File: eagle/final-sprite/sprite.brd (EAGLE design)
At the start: 35 x 44.6 mm, 60 parts, among them J1 M20-7910442R, U1 CC430F513X, U2 LSM9DS1, U4 DRV8837, U5 ADP5092, U6 DRV8837, U7 DRV8837, X1 SPRITEPIN_SPRITE_PIN, X2 SPRITEPIN_SPRITE_PIN

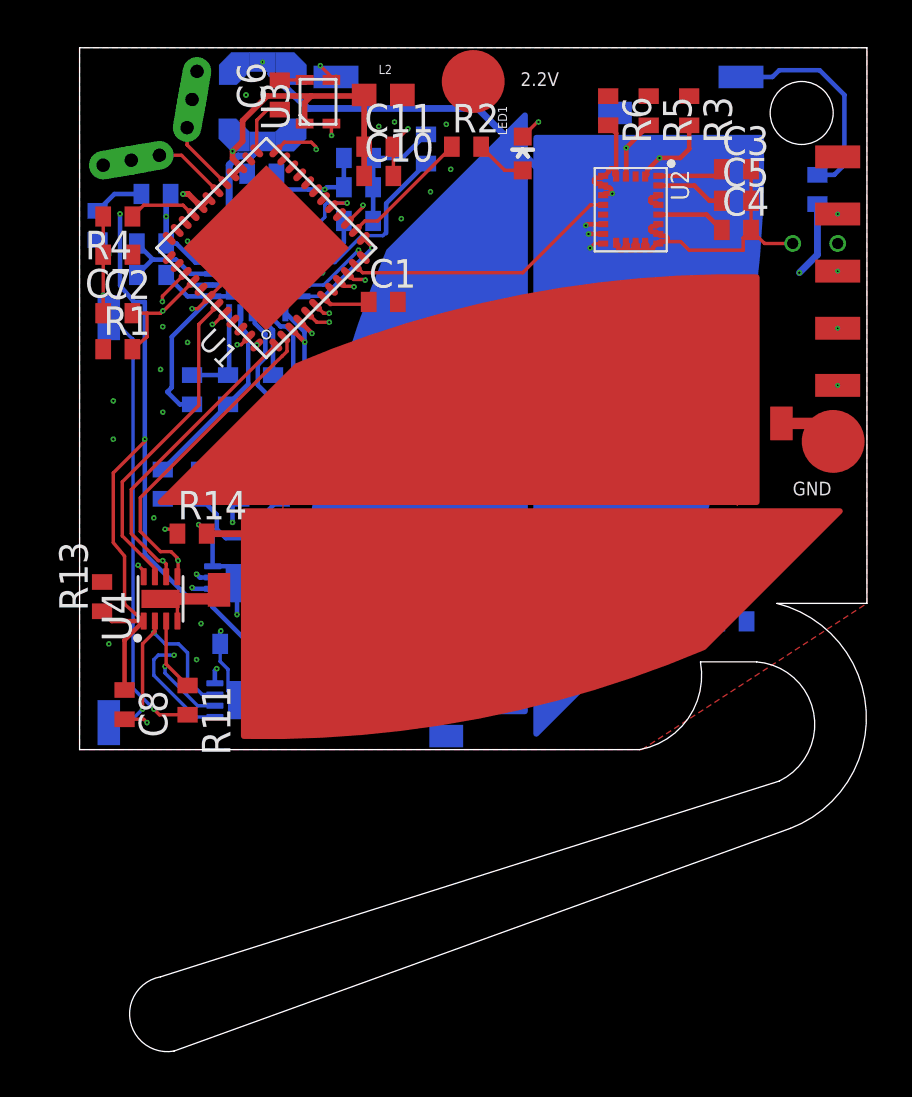
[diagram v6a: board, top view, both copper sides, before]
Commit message: moved all 3 drivers to the bottom side, removed the need for using interlayers and decreased the total number of vias
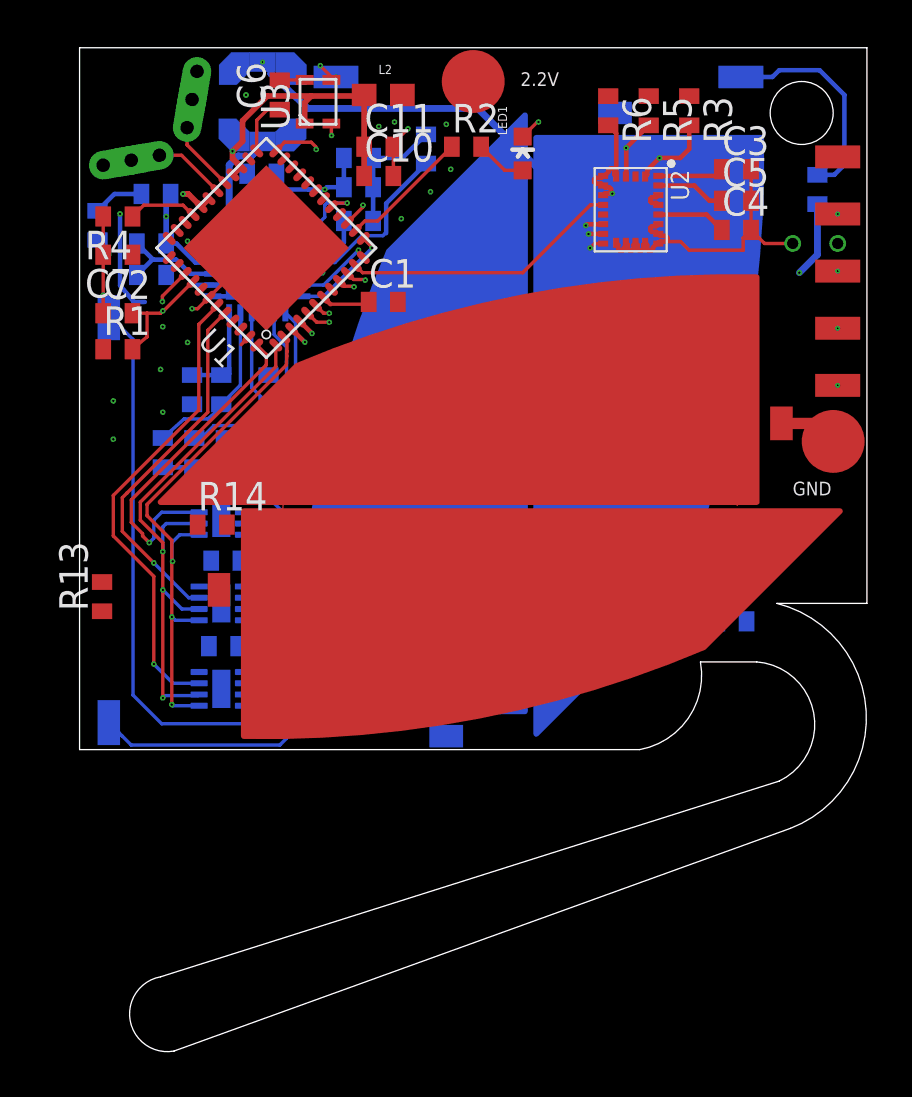
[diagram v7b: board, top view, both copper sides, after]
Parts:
- moved C8 5.11 mm to (6.40, 8.40), flipped to the bottom, turned to 0 degrees
- moved U4 4.83 mm to (6.30, 6.50), flipped to the bottom, turned to 0 degrees
- moved U6 4.36 mm to (6.30, 10.3)
- moved R11 3.72 mm to (8.50, 5.60), flipped to the bottom
- moved C12 3.72 mm to (6.50, 12.2)
- moved U7 2.96 mm to (6.30, 14.1), turned to 0 degrees
- moved R18 1.72 mm to (7.90, 17.0)
- moved R19 1.52 mm to (6.50, 17.0)
- moved R20 1.43 mm to (5.10, 17.0)
- moved R15 1.40 mm to (3.70, 17.0)
- moved R14 0.98 mm to (5.90, 13.8)
- moved R16 0.30 mm to (6.30, 19.8)
- moved R21 0.20 mm to (8.40, 19.8)
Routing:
- net GND: track 77.5 -> 46.9 mm, vias 11 -> 6
- net VCCIO: track 48.3 -> 27.6 mm, vias 3 -> 2
- net N$14: track 5.89 -> 13.1 mm, vias 1 -> 0
- net EN_1: track 14.4 -> 21.0 mm, vias 0 -> 1
- net PWM2: track 28.9 -> 24.2 mm
- net VCC: track 17.6 -> 13.3 mm, vias 21 -> 13
- net REF: track 16.8 -> 12.5 mm
- net PWM1: track 29.2 -> 25.0 mm
- net EN_2: track 20.4 -> 16.2 mm, vias 2 -> 1
- net N$4: track 19.9 -> 23.9 mm, vias 1 -> 0
- net VCCINT: track 41.0 -> 38.4 mm
- net N$8: track 3.26 -> 1.21 mm
- net TERM: track 9.99 -> 8.52 mm
- net SETSD: track 9.52 -> 8.12 mm
- net EN_3: track 14.1 -> 15.1 mm, vias 2 -> 1
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- removed copper zone on layer 2, net GND
- removed copper zone on layer 1, net VCC
- removed copper zone on layer 3, net VCC

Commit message: added new trisol footprint to layout
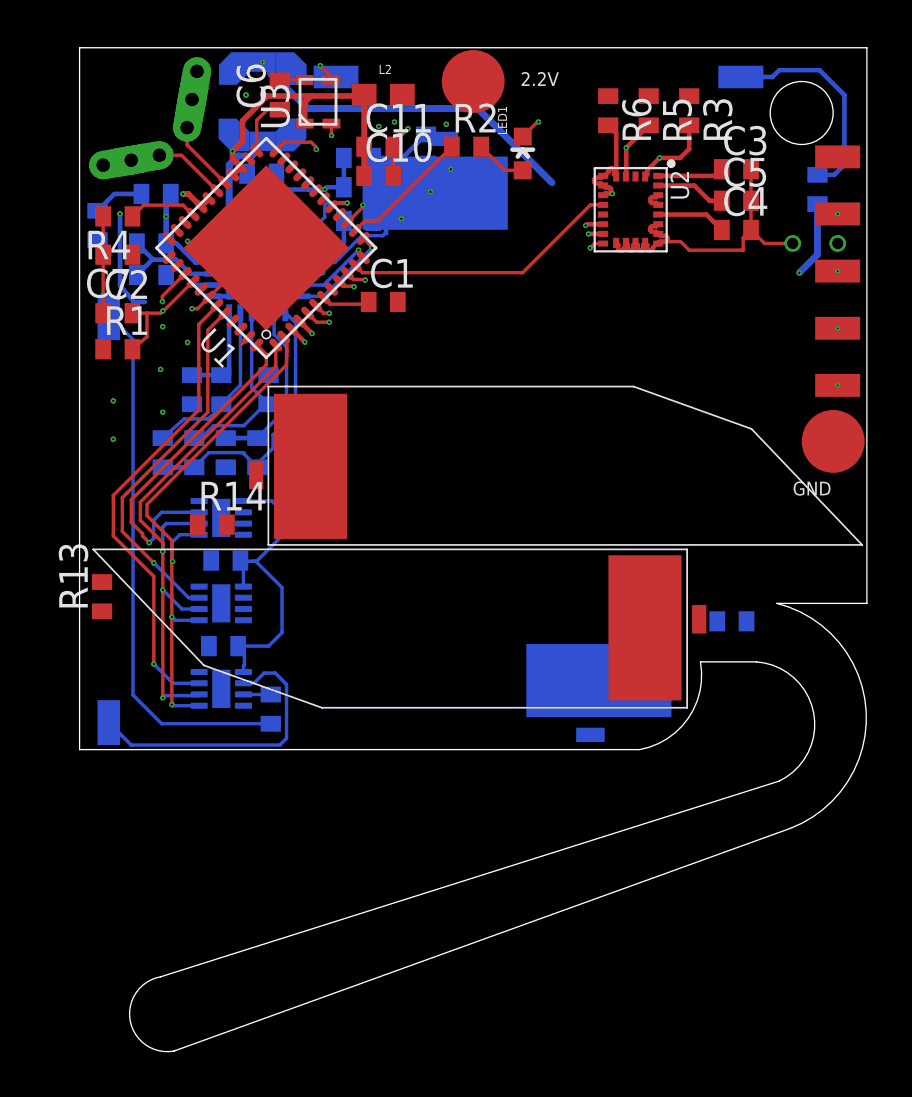
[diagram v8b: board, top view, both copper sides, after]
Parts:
- D1, D2, D3, D4: value TRISOLX-WING -> TRISOLX-WINGSTRAIGHT-RS; device STAC:TRISOLX_QZQUBE_TRISOLX-T01 -> STAC:TRISOLX-STRAIGHT-RS
- moved D4 14.2 mm to (22.2, 16.9)
- moved D3 13.4 mm to (16.7, 18.5)
- moved D2 9.82 mm to (20.3, 15.5)
- moved D1 8.91 mm to (15.1, 10.1)
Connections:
- net GND: now also D1.P$2, D2.P$2, D3.P$2, D4.P$2; no longer D1.P$3, D2.P$3, D3.P$3, D4.P$3
- net VCCINT: now also D1.P$1, D2.P$1, D3.P$1, D4.P$1; no longer D1.P$2, D2.P$2, D3.P$2, D4.P$2
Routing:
- net VCCINT: track 38.4 -> 29.7 mm
- net GND: track 46.9 -> 45.4 mm
- removed copper zone on layer 1, net VCCINT
- removed copper zone on layer 16, net VCCINT
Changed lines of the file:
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@@
 <element name="X2" library="STAC" package="SPRITEPIN_SPRITE_PIN" value="SPRITEPIN_SPRITE_PIN" x="33.5" y="17.5"/>
 <element name="B1" library="STAC" package="UMAC_UMAC" value="UMAC_UMAC" x="32.7" y="23.8" rot="MR90"/>
-<element name="D1" library="STAC" package="TRISOLX_QZQUBE_TRISOLX-T01" value="TRISOLX-WING" x="7.3" y="14.4" rot="R180"/>
-<element name="D2" library="STAC" package="TRISOLX_QZQUBE_TRISOLX-T01" value="TRISOLX-WING" x="30.1" y="14.8"/>
-<element name="D3" library="STAC" package="TRISOLX_QZQUBE_TRISOLX-T01" value="TRISOLX-WING" x="19.8" y="5.5" rot="MR270"/>
-<element name="D4" library="STAC" package="TRISOLX_QZQUBE_TRISOLX-T01" value="TRISOLX-WING" x="20.3" y="31" rot="MR90"/>
+<element name="D2" library="STAC" package="TRISOLX-STRAIGHT-RS" value="TRISOLX-WINGSTRAIGHT-RS" x="20.3" y="15.5"/>
+<element name="D3" library="STAC" package="TRISOLX-STRAIGHT-RS" value="TRISOLX-WINGSTRAIGHT-RS" x="16.7" y="18.5" rot="MR270"/>
+<element name="D4" library="STAC" package="TRISOLX-STRAIGHT-RS" value="TRISOLX-WINGSTRAIGHT-RS" x="22.2" y="16.9" rot="MR90"/>
 <element name="U3" library="STAC" package="SPRITETCXO_TXC_7Z" value="" x="10.6" y="32.6" rot="R90"/>
 <element name="U1" library="STAC" package="TI_MSP430_V16_RGZ48" value="CC430F513X" x="8.3" y="26.1" rot="R135"/>
@@
 <element name="L3" library="STAC" package="PCBSAT-TORQUECOIL" value="PCBSAT-TORQUECOIL" x="1.3" y="14" rot="MR270"/>
 <element name="L4" library="STAC" package="PCBSAT-TORQUECOIL" value="PCBSAT-TORQUECOIL" x="20.4" y="33.7" rot="MR0"/>
+<element name="D1" library="STAC" package="TRISOLX-STRAIGHT-RS" value="TRISOLX-WINGSTRAIGHT-RS" x="15.1" y="10.1" rot="R180"/>
 </elements>
 <signals>
@@
 <contactref element="X2" pad="PIN"/>
 <contactref element="B1" pad="V-"/>
-<contactref element="D1" pad="P$3"/>
-<contactref element="D2" pad="P$3"/>
-<contactref element="D3" pad="P$3"/>
-<contactref element="D4" pad="P$3"/>
+<contactref element="D2" pad="P$2"/>
+<contactref element="D3" pad="P$2"/>
+<contactref element="D4" pad="P$2"/>
 <contactref element="U3" pad="GND2"/>
 <contactref element="U3" pad="GND1"/>
@@
 <wire x1="26.717" y1="26.383" x2="27.1" y2="26" width="0.1524" layer="1"/>
 <wire x1="33.5" y1="17.5" x2="32.7" y2="18.3" width="0.508" layer="1"/>
-<wire x1="32.7" y1="18.3" x2="31.2" y2="18.3" width="0.508" layer="1"/>
 <wire x1="29.85" y1="26.9" x2="30.45" y2="26.3" width="0.1524" layer="1"/>
 <wire x1="30.45" y1="26.3" x2="31.7" y2="26.3" width="0.1524" layer="1"/>
@@
 <wire x1="11.195" y1="33.705" x2="10.7" y2="34.2" width="0.1524" layer="1"/>
 <via x="10.7" y="34.2" extent="1-2" drill="0.1016"/>
-<wire x1="20.4" y1="31.7" x2="23.8" y2="32.1" width="0" layer="19" extent="2-16"/>
+<contactref element="D1" pad="P$2"/>
+<wire x1="33.5" y1="17.5" x2="33.7" y2="17.45" width="0" layer="19" extent="1-1"/>
+<wire x1="31.7" y1="26.3" x2="32.7" y2="18.3" width="0" layer="19" extent="1-1"/>
+<wire x1="23.089" y1="6.867" x2="24.01739375" y2="25.973" width="0" layer="19" extent="1-16"/>
+<wire x1="15.811" y1="28.533" x2="23.089" y2="6.867" width="0" layer="19" extent="16-16"/>
+<wire x1="19.7" y1="31.05" x2="23.855" y2="26.325" width="0" layer="19" extent="1-1"/>
 <wire x1="15.4" y1="31.15" x2="19.7" y2="31.05" width="0" layer="19" extent="1-16"/>
 <wire x1="13.95" y1="30.6" x2="14.35" y2="30.1" width="0" layer="19" extent="1-16"/>
@@
 <wire x1="7.285" y1="13.35" x2="6.3" y2="14.1" width="0" layer="19" extent="16-16"/>
 <wire x1="5.85" y1="12.2" x2="7.285" y2="13.35" width="0" layer="19" extent="16-16"/>
-<wire x1="6.2" y1="10.9" x2="5.85" y2="12.2" width="0" layer="19" extent="1-16"/>
-<wire x1="6.3" y1="10.3" x2="6.2" y2="10.9" width="0" layer="19" extent="1-16"/>
+<wire x1="6.3" y1="10.3" x2="5.85" y2="12.2" width="0" layer="19" extent="16-16"/>
 <wire x1="7.285" y1="9.55" x2="6.3" y2="10.3" width="0" layer="19" extent="16-16"/>
 <wire x1="5.75" y1="8.4" x2="7.285" y2="9.55" width="0" layer="19" extent="16-16"/>
@@
 <wire x1="7.285" y1="5.75" x2="6.3" y2="6.5" width="0" layer="19" extent="16-16"/>
 <wire x1="14.15" y1="23.7" x2="13.05" y2="27.3" width="0" layer="19" extent="1-16"/>
-<wire x1="25.44739375" y1="27.067" x2="23.8" y2="32.1" width="0" layer="19" extent="1-16"/>
-<wire x1="31.2" y1="18.3" x2="29.5" y2="26" width="0" layer="19" extent="1-1"/>
-<wire x1="33.7" y1="17.45" x2="33.5" y2="17.5" width="0" layer="19" extent="1-1"/>
-<wire x1="16.3" y1="4.4" x2="7.285" y2="5.75" width="0" layer="19" extent="16-16"/>
+<wire x1="10.267" y1="16.389" x2="6.5" y2="16.35" width="0" layer="19" extent="1-16"/>
+<wire x1="25.133" y1="9.211" x2="7.285" y2="5.75" width="0" layer="19" extent="1-16"/>
 </signal>
 <signal name="N$3">
@@
 <contactref element="C17" pad="1"/>
 <contactref element="R14" pad="2"/>
-<contactref element="D1" pad="P$2"/>
-<contactref element="D2" pad="P$2"/>
-<contactref element="D3" pad="P$2"/>
-<contactref element="D4" pad="P$2"/>
+<contactref element="D2" pad="P$1"/>
+<contactref element="D3" pad="P$1"/>
+<contactref element="D4" pad="P$1"/>
 <wire x1="3.85" y1="26.3" x2="3.85" y2="27.5" width="0.254" layer="16"/>
 <wire x1="4.05" y1="28.5" x2="3.85" y2="28.3" width="0.254" layer="16"/>
@@
 <wire x1="8.509903125" y1="33.843653125" x2="8.51289375" y2="33.8406625" width="0.3048" layer="16"/>
 <wire x1="8.5735375" y1="33.78001875" x2="10.15355625" y2="32.3" width="0.3048" layer="16"/>
-<wire x1="21" y1="29" x2="25.3" y2="29" width="0.3048" layer="16"/>
 <wire x1="10.15355625" y1="32.3" x2="17.7" y2="32.3" width="0.3048" layer="16"/>
 <wire x1="17.7" y1="32.3" x2="21" y2="29" width="0.3048" layer="16"/>
-<polygon width="0.3048" layer="16">
-<vertex x="19.8" y="31"/>
-<vertex x="25.9" y="29.5"/>
-<vertex x="25.5" y="10.6"/>
-<vertex x="13" y="6.3"/>
-<vertex x="19.9" y="30.9"/>
-</polygon>
-<polygon width="0.3048" layer="1" thermals="no">
-<vertex x="8.3" y="5.5"/>
-<vertex x="9.5" y="20.2"/>
-<vertex x="29.3" y="21.3"/>
-<vertex x="29.2" y="11"/>
-</polygon>
 <wire x1="5.92" y1="25.45" x2="5.15" y2="25.45" width="0.2032" layer="16"/>
 <wire x1="4.3" y1="26.3" x2="3.85" y2="26.3" width="0.2032" layer="16"/>
 <wire x1="5.15" y1="25.45" x2="4.3" y2="26.3" width="0.2032" layer="16"/>
-<wire x1="8.2" y1="13.4" x2="8.2" y2="10.5" width="0.3048" layer="1"/>
-<wire x1="8.2" y1="10.5" x2="9.3" y2="9.4" width="0.3048" layer="1"/>
-<wire x1="25.3" y1="29" x2="28.1" y2="19.8" width="0" layer="19" extent="1-16"/>
-<wire x1="6.55" y1="13.8" x2="5.92" y2="25.45" width="0" layer="19" extent="1-16"/>
-<wire x1="8.2" y1="13.4" x2="6.55" y2="13.8" width="0" layer="19" extent="1-1"/>
-<wire x1="14.8" y1="7.5" x2="9.3" y2="9.4" width="0" layer="19" extent="1-16"/>
+<contactref element="D1" pad="P$1"/>
+<wire x1="17.7" y1="32.3" x2="16.192" y2="30.946" width="0" layer="19" extent="16-16"/>
+<wire x1="7.854" y1="16.008" x2="5.92" y2="25.45" width="0" layer="19" extent="1-16"/>
+<wire x1="6.55" y1="13.8" x2="7.854" y2="16.008" width="0" layer="19" extent="1-1"/>
+<wire x1="22.708" y1="4.454" x2="6.55" y2="13.8" width="0" layer="19" extent="1-16"/>
+<wire x1="27.546" y1="9.592" x2="22.708" y2="4.454" width="0" layer="19" extent="1-16"/>
 </signal>
 <signal name="VBAT">
